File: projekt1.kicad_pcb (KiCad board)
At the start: 2 copper layers, 94 parts, among them IC1 TPS563300DRLR, J1 V1, J2 V1, K1 1461103-1, K2 SANYOU_SRD_Form_B, Q1 MMBT3904, Q2 MMBT3904, SW1 SW_Push, SW10 SW_Push, SW11 SW_Push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

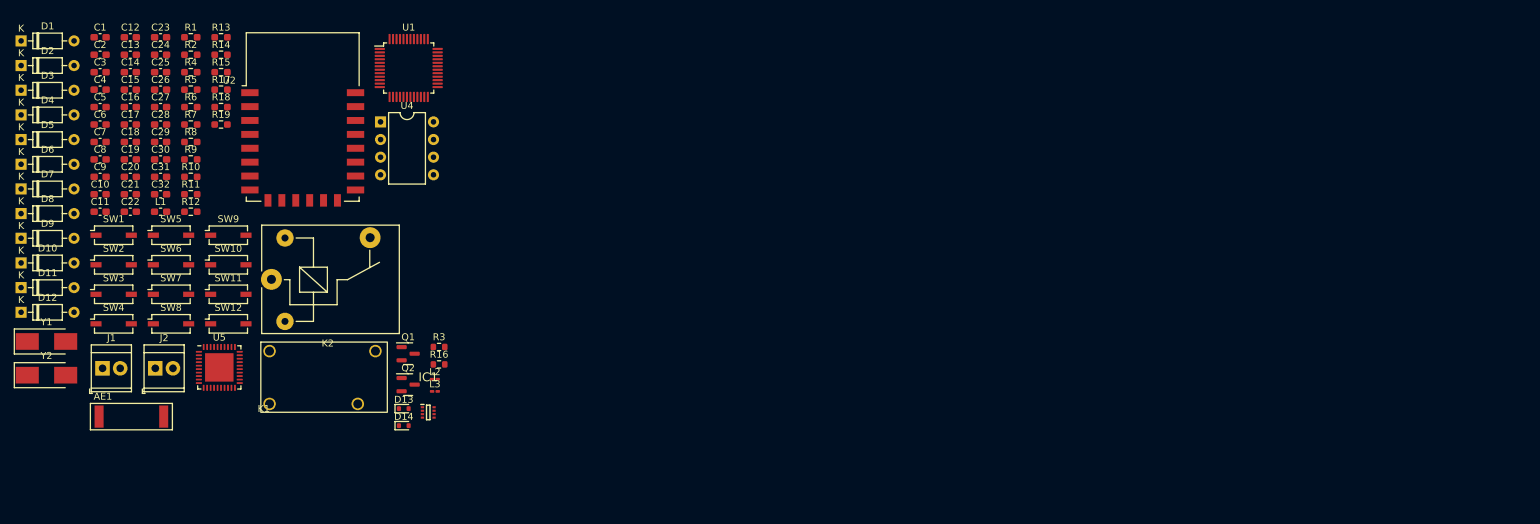
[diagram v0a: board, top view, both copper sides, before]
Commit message: initial pcb elements arrangement
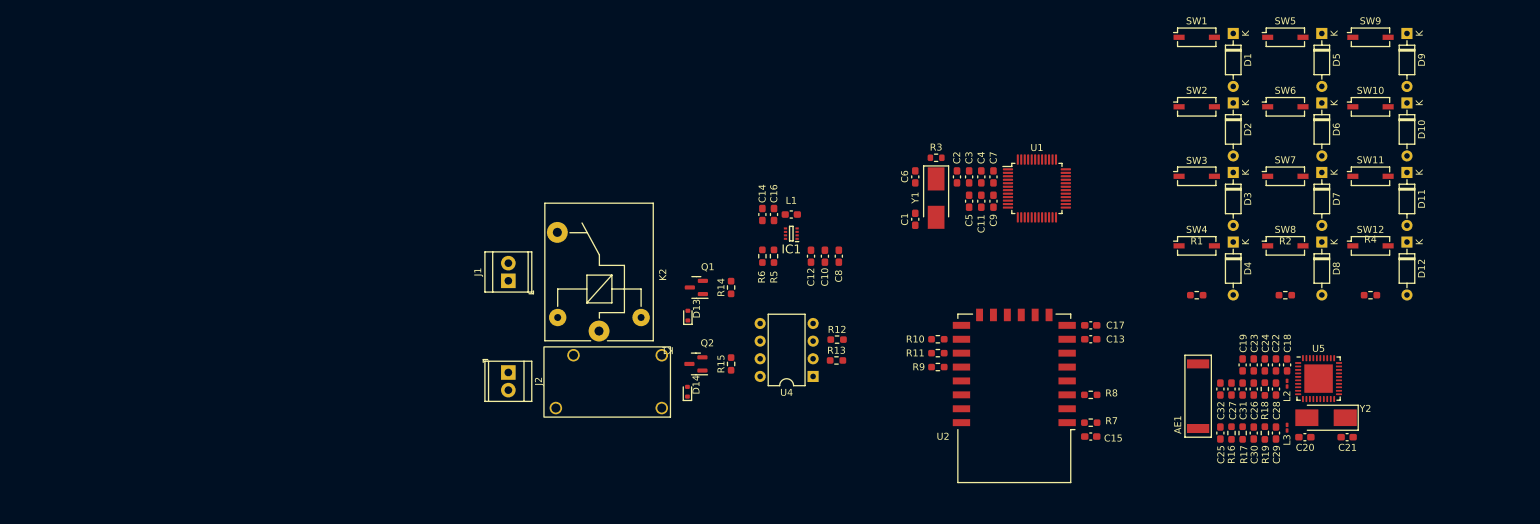
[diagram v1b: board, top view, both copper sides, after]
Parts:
- R16: footprint Resistor_SMD:R_0603_1608Metric -> Resistor_SMD:R_0603_1608Metric_Pad0.98x0.95mm_HandSolder
- moved D9 201.6 mm to (243.2, 56.5), turned to -90 degrees
- moved D10 200.7 mm to (243.2, 66.5), turned to -90 degrees
- moved D11 200.1 mm to (243.2, 76.5), turned to -90 degrees
- moved D12 199.7 mm to (243.2, 86.5), turned to -90 degrees
- moved D5 187.8 mm to (231.0, 56.5), turned to -90 degrees
- moved D6 187.4 mm to (231.0, 66.5), turned to -90 degrees
- moved D8 187.2 mm to (231.0, 86.5), turned to -90 degrees
- moved D7 187.2 mm to (231.0, 76.5), turned to -90 degrees
- moved Y2 184.2 mm to (231.6, 111.7), turned to 180 degrees
- moved C21 178.5 mm to (234.6, 114.5)
- moved D4 175.4 mm to (218.2, 86.5), turned to -90 degrees
- moved D3 174.8 mm to (218.2, 76.5), turned to -90 degrees
- moved D2 174.5 mm to (218.2, 66.5), turned to -90 degrees
- moved D1 174.4 mm to (218.2, 56.5), turned to -90 degrees
- moved C20 173.1 mm to (228.6, 114.5)
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
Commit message: pcb connections implemented
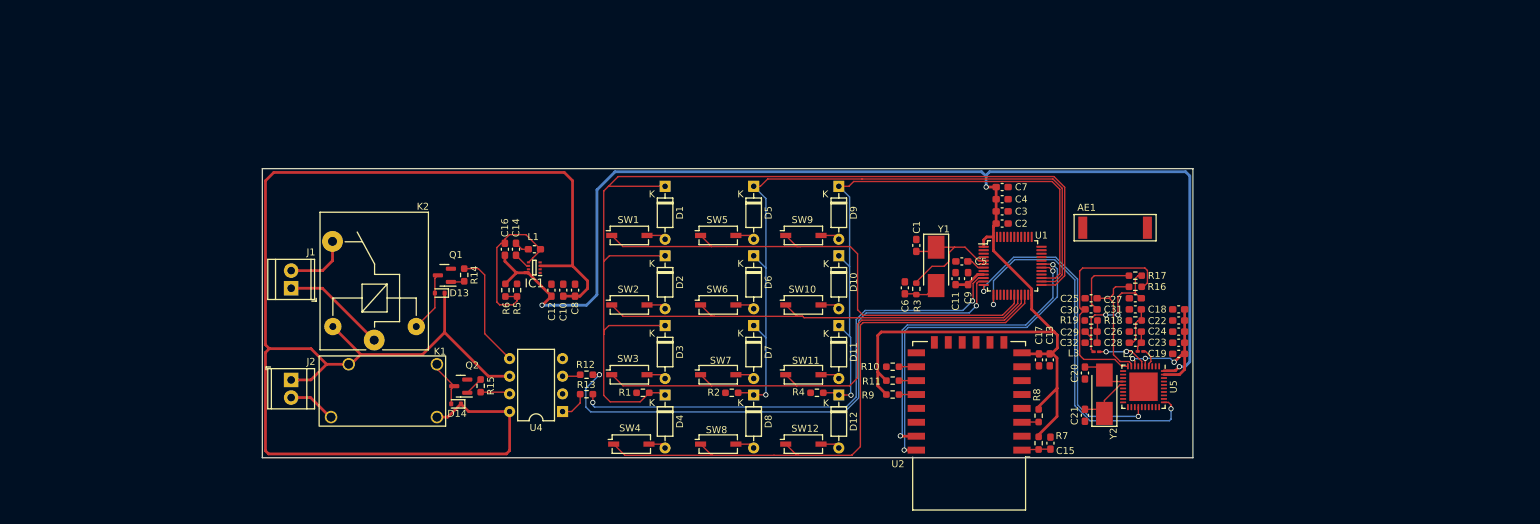
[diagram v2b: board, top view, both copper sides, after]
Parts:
- moved SW3 86.5 mm to (131.4, 105.5)
- moved SW1 86.5 mm to (131.4, 85.5)
- moved SW2 86.5 mm to (131.4, 95.5)
- moved SW11 86.5 mm to (156.4, 105.5)
- moved SW7 86.5 mm to (144.2, 105.5)
- moved SW12 86.4 mm to (156.4, 115.5)
- moved SW8 86.4 mm to (144.2, 115.5)
- moved SW10 86.4 mm to (156.4, 95.5)
- moved SW5 86.4 mm to (144.2, 85.5)
- moved SW6 86.4 mm to (144.2, 95.5)
- moved SW9 86.4 mm to (156.4, 85.5)
- moved SW4 86.2 mm to (131.6, 115.5)
- moved D11 84.7 mm to (161.5, 98.5)
- moved D3 84.7 mm to (136.5, 98.5)
- moved D7 84.7 mm to (149.2, 98.5)
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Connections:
- D13 pad 1: /COM_V2 -> +24V
- K2 pad 5: /COM_V2 -> +24V
- U1 pad 19: unconnected-(U1-PB1-Pad19) -> /ROW0
- U1 pad 20: unconnected-(U1-PB2-Pad20) -> /ROW1
- U1 pad 45: /ROW0 -> unconnected-(U1-PB8-Pad45)
- U1 pad 46: /ROW1 -> unconnected-(U1-PB9-Pad46)
- U4 pad 6: /COM_V2 -> +24V
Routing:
- net VDD: track 0.00 -> 248.7 mm, vias 0 -> 3
- net +24V: track 0.00 -> 219.9 mm
- net /COL0: track 0.00 -> 150.7 mm
- net /COL1: track 0.00 -> 101.2 mm, vias 0 -> 1
- net /COL2: track 0.00 -> 86.9 mm, vias 0 -> 1
- net /ROW3: track 0.00 -> 85.3 mm
- net /V2_Close: track 0.00 -> 80.3 mm, vias 0 -> 2
- net /ROW2: track 0.00 -> 74.8 mm
- net /ROW0: track 0.00 -> 74.4 mm
- net /V1_Open: track 0.00 -> 73.6 mm, vias 0 -> 2
- net /ROW1: track 0.00 -> 67.1 mm
- net /USART2_Rx: track 0.00 -> 55.1 mm, vias 0 -> 2
- net /USART1_Rx: track 0.00 -> 49.8 mm, vias 0 -> 2
- net /USART2_Tx: track 0.00 -> 47.0 mm, vias 0 -> 2
- net /USART1_Tx: track 0.00 -> 47.0 mm, vias 0 -> 2
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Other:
- board outline added: 133.9 x 41.6 mm

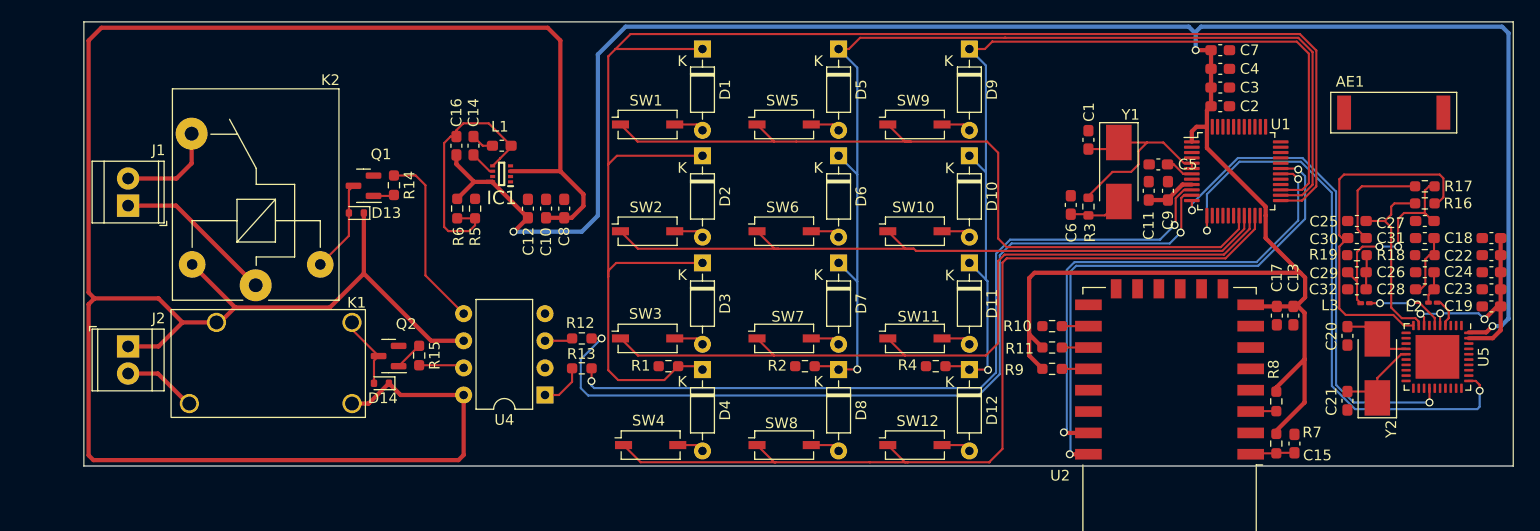
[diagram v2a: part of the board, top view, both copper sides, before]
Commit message: changed connector footprint and adjusted paths width
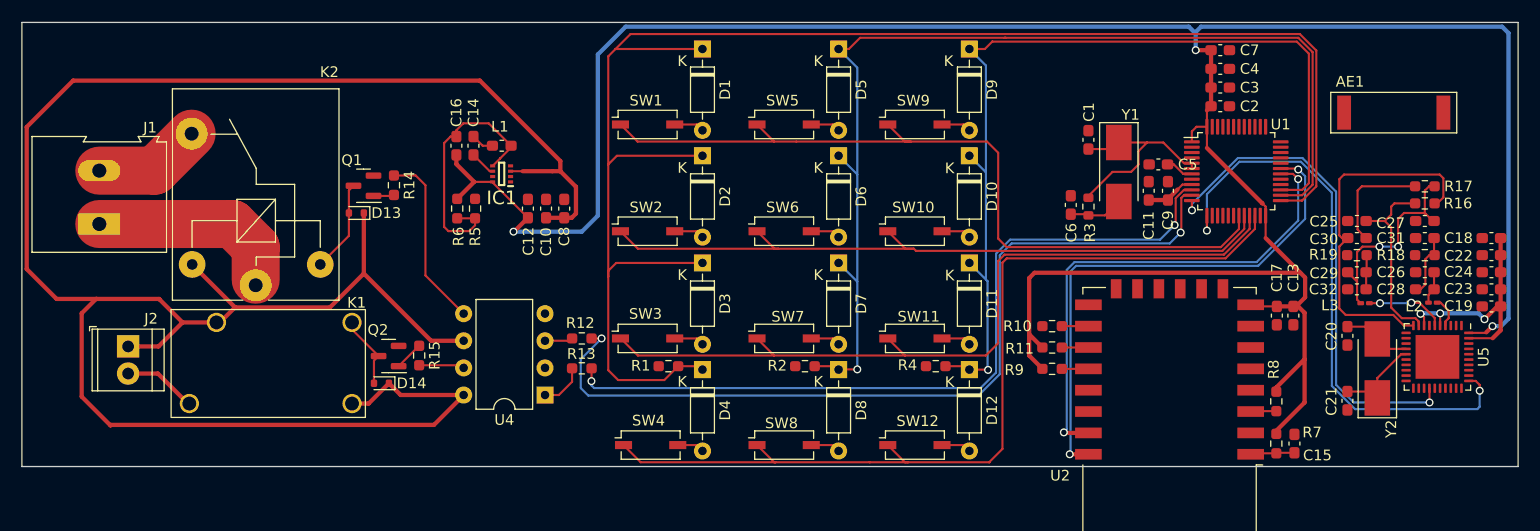
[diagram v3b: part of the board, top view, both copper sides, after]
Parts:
- J1: footprint TerminalBlock_TE-Connectivity:TerminalBlock_TE_282834-2_1x02_P2.54mm_Horizontal -> TerminalBlock:TerminalBlock_Altech_AK300-2_P5.00mm
- moved J1 3.20 mm to (80.0, 94.8)
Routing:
- net +24V: track 219.9 -> 206.0 mm
- net /COM_V2: track 15.0 -> 18.6 mm
- net /Relay2_NC: track 9.32 -> 10.1 mm
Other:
- board size 133.9 x 41.6 mm -> 140.2 x 41.6 mm

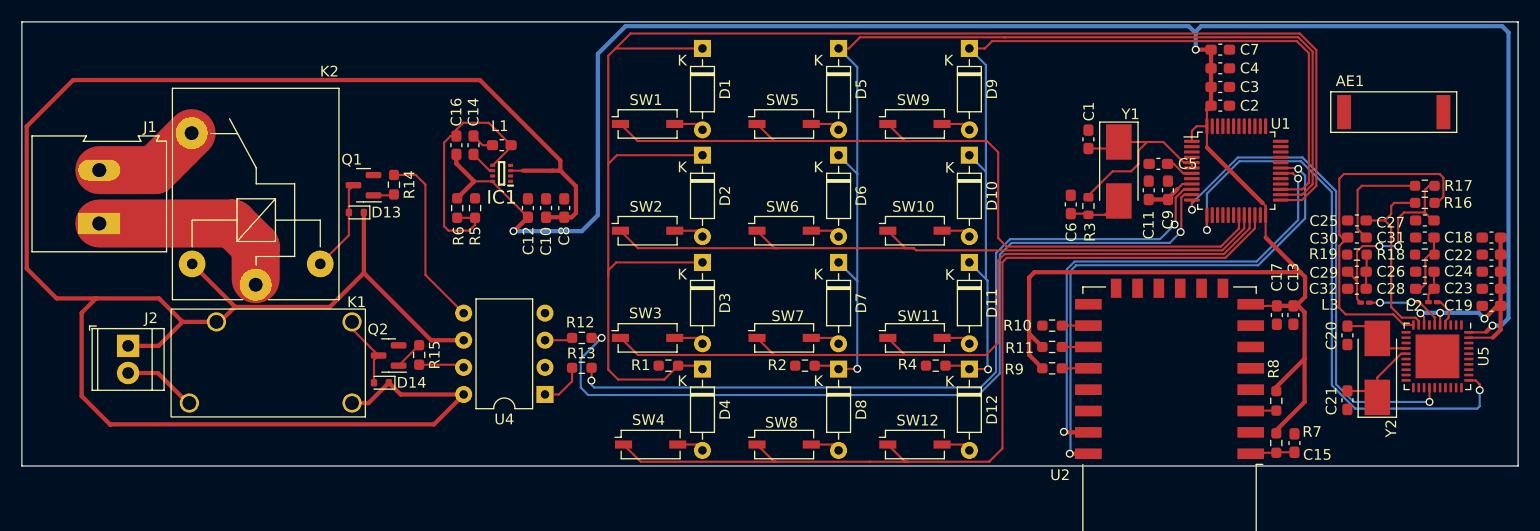
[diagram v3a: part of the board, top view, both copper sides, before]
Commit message: add external rfid module connectors
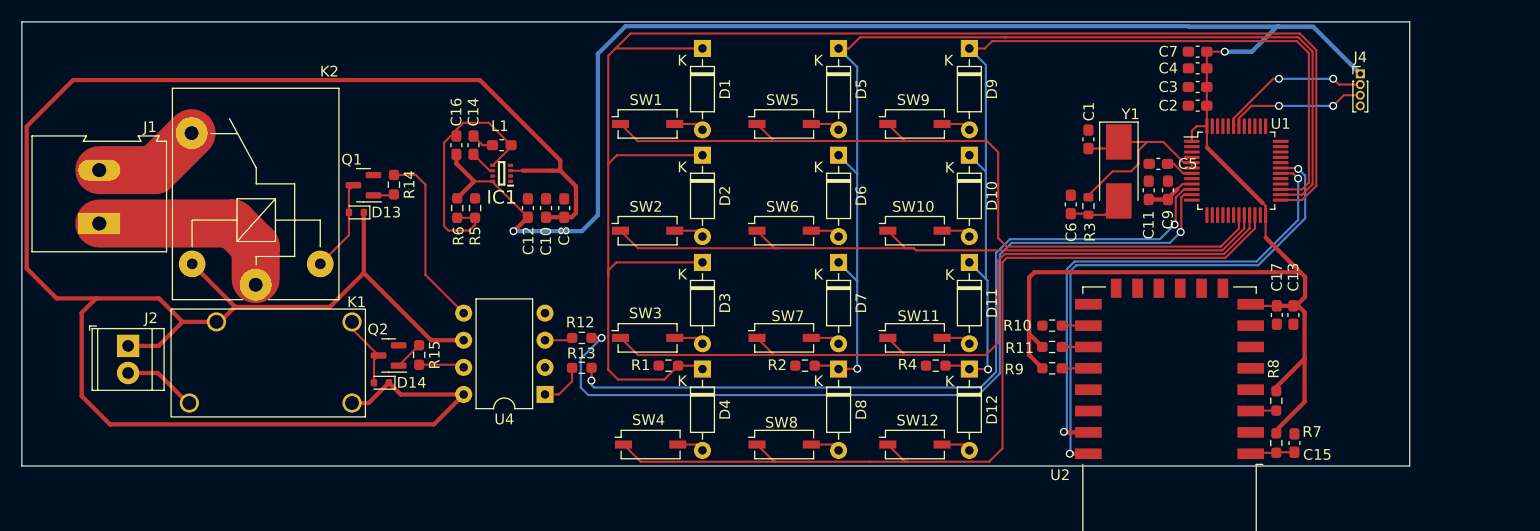
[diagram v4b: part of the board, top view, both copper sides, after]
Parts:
- removed AE1: Antenna, RF_Antenna:Coilcraft_MA5532-AE_RFID
- removed C18, C19: 4.7uF, Capacitor_SMD:C_0603_1608Metric_Pad1.08x0.95mm_HandSolder
- removed C20, C21: 22pF, Capacitor_SMD:C_0603_1608Metric_Pad1.08x0.95mm_HandSolder
- removed C22, C23, C24, C25: 100nF, Capacitor_SMD:C_0603_1608Metric_Pad1.08x0.95mm_HandSolder
- removed C26, C27: 220pF, Capacitor_SMD:C_0603_1608Metric_Pad1.08x0.95mm_HandSolder
- removed C28, C29, C31, C32: 150pF, Capacitor_SMD:C_0603_1608Metric_Pad1.08x0.95mm_HandSolder
- removed C30: 1nF, Capacitor_SMD:C_0603_1608Metric_Pad1.08x0.95mm_HandSolder
- removed L2, L3: 560nH, Inductor_SMD:L_0201_0603Metric_Pad0.64x0.40mm_HandSolder
- removed R16: 1k, Resistor_SMD:R_0603_1608Metric_Pad0.98x0.95mm_HandSolder
- removed R17: 2.7k, Resistor_SMD:R_0603_1608Metric_Pad0.98x0.95mm_HandSolder
- removed R18, R19: 10, Resistor_SMD:R_0603_1608Metric_Pad0.98x0.95mm_HandSolder
- removed U5: PN5321A3HN_C1xx, Package_DFN_QFN:HVQFN-40-1EP_6x6mm_P0.5mm_EP4.1x4.1mm
- removed Y2: 27.12MHz1, Crystal:Crystal_SMD_Abracon_ABM3-2Pin_5.0x3.2mm_HandSoldering
- added J4: Conn_01x04_Pin, Connector_PinHeader_1.00mm:PinHeader_1x04_P1.00mm_Vertical, F.Cu at (198.1, 80.8)
- moved C7 2.13 mm to (182.9, 78.7), turned to 180 degrees
- moved C2 2.12 mm to (182.9, 83.8), turned to 180 degrees
- moved C3 2.12 mm to (182.9, 82.0), turned to 180 degrees
- moved C4 2.12 mm to (182.9, 80.3), turned to 180 degrees
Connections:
- U1 pad 12: /USART2_Tx -> unconnected-(U1-PA2-Pad12)
- U1 pad 13: /USART2_Rx -> unconnected-(U1-PA3-Pad13)
- U1 pad 42: unconnected-(U1-PB6-Pad42) -> /I2C1_SCL
- U1 pad 43: unconnected-(U1-PB7-Pad43) -> /I2C1_SDA
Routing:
- net /USART2_Rx: track 55.1 -> 0.00 mm, vias 2 -> 0
- net /USART2_Tx: track 47.0 -> 0.00 mm, vias 2 -> 0
- net VDD: track 248.7 -> 209.2 mm, vias 3 -> 2
- net Net-(U5-RX): track 33.6 -> 0.00 mm
- net /DVDD: track 22.7 -> 0.00 mm, vias 3 -> 0
- net Net-(C27-Pad2): track 19.9 -> 0.00 mm, vias 2 -> 0
- net Net-(U5-VMID): track 17.6 -> 0.00 mm
- net /I2C1_SDA: track 0.00 -> 14.5 mm, vias 0 -> 2
- net /I2C1_SCL: track 0.00 -> 13.0 mm, vias 0 -> 2
- net Net-(C30-Pad2): track 10.3 -> 0.00 mm
- net Net-(U5-OSCOUT): track 8.53 -> 0.00 mm
- net Net-(U5-TX2): track 7.44 -> 0.00 mm, vias 2 -> 0
- net Net-(U5-OSCIN): track 6.81 -> 0.00 mm
- net Net-(C28-Pad2): track 6.11 -> 0.00 mm
- net Net-(C26-Pad1): track 3.48 -> 0.00 mm
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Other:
- board size 140.2 x 41.6 mm -> 130 x 41.6 mm

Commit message: rfid module
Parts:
- removed J4: Conn_01x04_Pin, Connector_PinHeader_1.00mm:PinHeader_1x04_P1.00mm_Vertical
- added P1: RFID-RC522-MODULE, RF_Module:ESP-07, F.Cu at (207.5, 94.0)
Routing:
- net /I2C1_SDA: track 14.5 -> 31.1 mm
- net /I2C1_SCL: track 13.0 -> 27.2 mm
- net VDD: track 209.2 -> 214.9 mm, vias 2 -> 3
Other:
- board size 130 x 41.6 mm -> 142.7 x 41.6 mm

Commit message: rc522
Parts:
- removed P1: RFID-RC522-MODULE, RF_Module:ESP-07
- added RFID1: RC522, My_Footprints_Library:RC522_I2C_B30x20mm, F.Cu at (198.7, 76.6)
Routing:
- net VDD: track 214.9 -> 235.5 mm
- net /I2C1_SDA: track 31.1 -> 23.0 mm
- net /I2C1_SCL: track 27.2 -> 23.5 mm

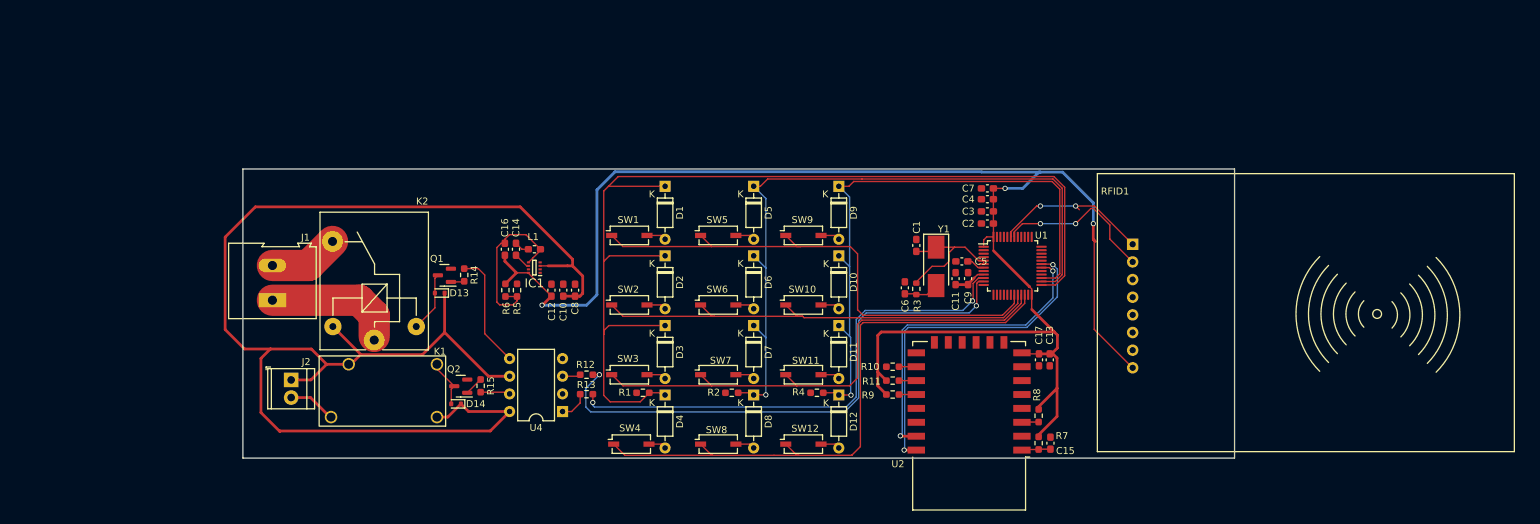
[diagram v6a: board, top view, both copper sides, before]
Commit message: add text to footprint
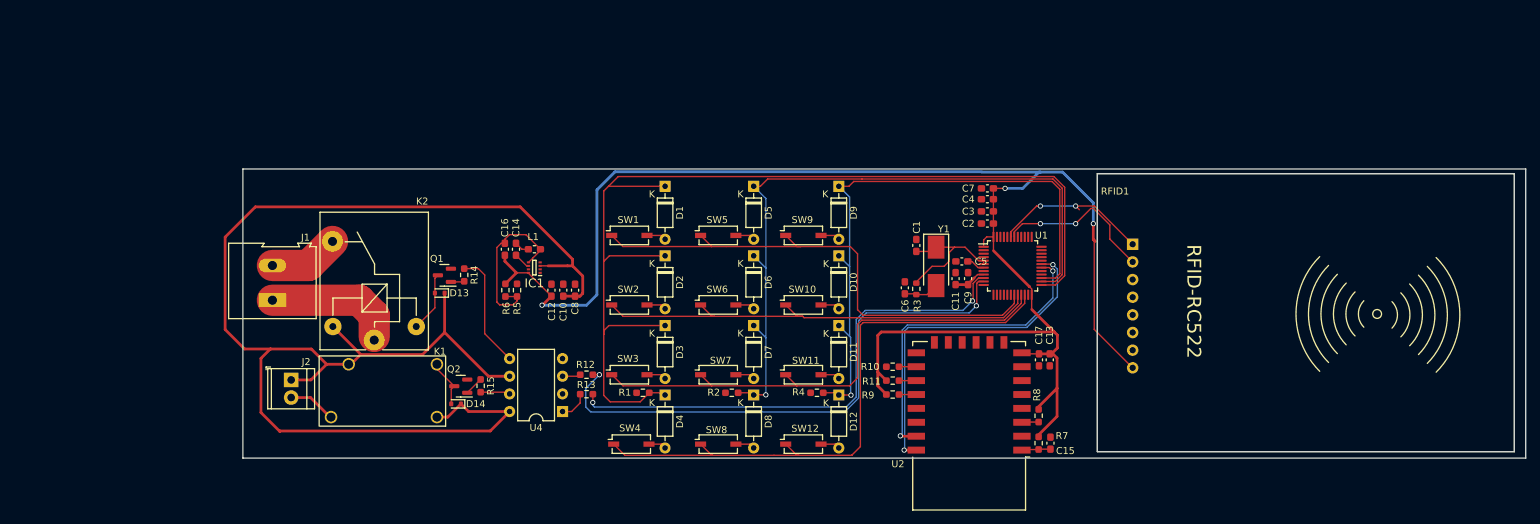
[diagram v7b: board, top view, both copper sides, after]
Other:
- board size 142.7 x 41.6 mm -> 184.6 x 41.6 mm
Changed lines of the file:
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@@
         (effects (font (size 1 1) (thickness 0.15)))
+    )
+    (fp_text user "RFID-RC522" (at 12.7 10.16 270 unlocked) (layer "F.SilkS")
+        (effects (font (size 2 2) (thickness 0.1)) (justify left bottom))
     )
     (fp_line (start 0 0) (end 0 40)
@@
     (fp_circle (center 40.254027 20.189689) (end 40.889027 20.189689)
       (stroke (width 0.1) (type solid)) (fill none) (layer "F.SilkS"))
+    (fp_line (start 0 0) (end 60 0)
+      (stroke (width 0.05) (type default)) (layer "Edge.Cuts"))
+    (fp_line (start 0 40) (end 0 0)
+      (stroke (width 0.05) (type default)) (layer "Edge.Cuts"))
+    (fp_line (start 60 0) (end 60 40)
+      (stroke (width 0.05) (type default)) (layer "Edge.Cuts"))
+    (fp_line (start 60 40) (end 0 40)
+      (stroke (width 0.05) (type default)) (layer "Edge.Cuts"))
     (pad "1" thru_hole rect (at 5.08 10.16) (size 1.65 1.65) (drill 0.9) (layers "*.Cu" "*.Mask")
       (net 13 "/I2C1_SDA") (pinfunction "SDA") (pintype "output"))
@@
     )
   )
-  (gr_rect (start 75.75 75.95) (end 218.44 117.55)
+  (gr_rect (start 75.75 75.95) (end 260.34 117.55)
     (stroke (width 0.1) (type default)) (fill none) (layer "Edge.Cuts"))
   (segment (start 178.15 87.2) (end 175.5 87.2) (width 0.2) (layer "F.Cu") (net 2))

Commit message: dla patryka kochaniutkiego
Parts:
- moved RFID1 2.20 mm to (196.5, 76.7)
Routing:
- net VDD: track 235.5 -> 198.9 mm, vias 3 -> 2
- net /I2C1_SCL: track 23.5 -> 18.4 mm
- net /I2C1_SDA: track 23.0 -> 20.1 mm
